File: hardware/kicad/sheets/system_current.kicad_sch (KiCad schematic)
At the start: 5 parts, among them U23 INA237AIDGSR

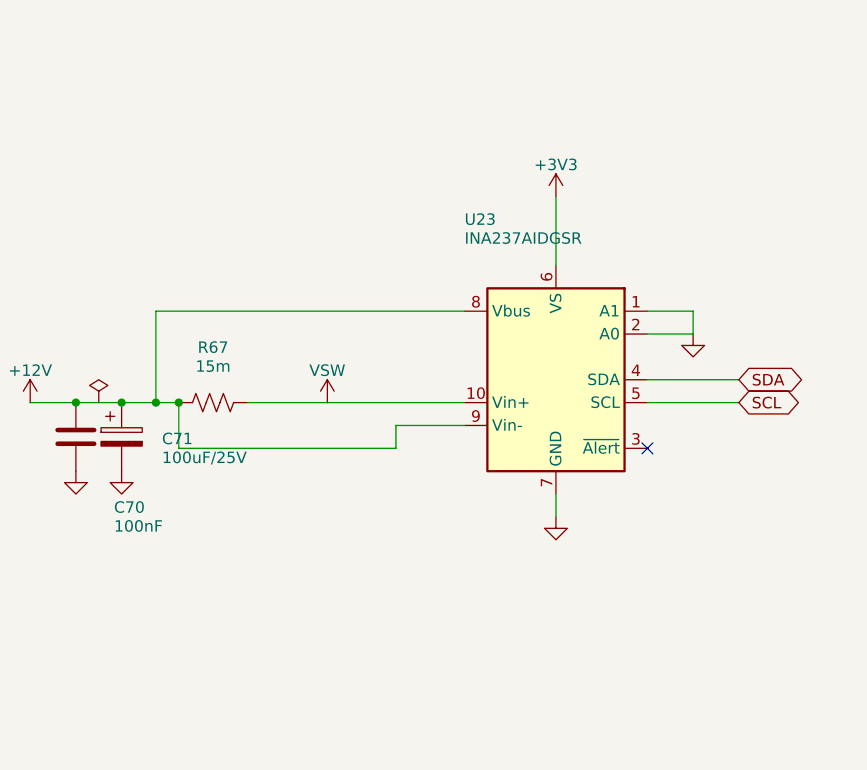
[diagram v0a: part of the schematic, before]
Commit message: Put supply pins on top and grounds on the bottom of IC symbols; flake8-clean Python
Schematic: re-laid out pins on U2, U3, U6, U7, U11, U14, U17-U20, U22-U24
and PS1 (supply on top, ground/strap pins on the bottom edge) via custom
`cryocooler:` symbols (make_lib.from_stock) and a gnd_bus helper; U18/U2
use mirroring instead of a 180 degree rotation. Nets are unchanged (ERC 0,
117/117 datasheet rules, PCB nets still match). Text placement now shows
every power-symbol name, avoids wires, and uses a realistic character width.

Python: black -l 79 -S plus manual wrapping so hardware/kicad and scripts/
pass flake8; add .flake8.

Co-Authored-By: Claude Sonnet 5.5 <noreply@anthropic.com>
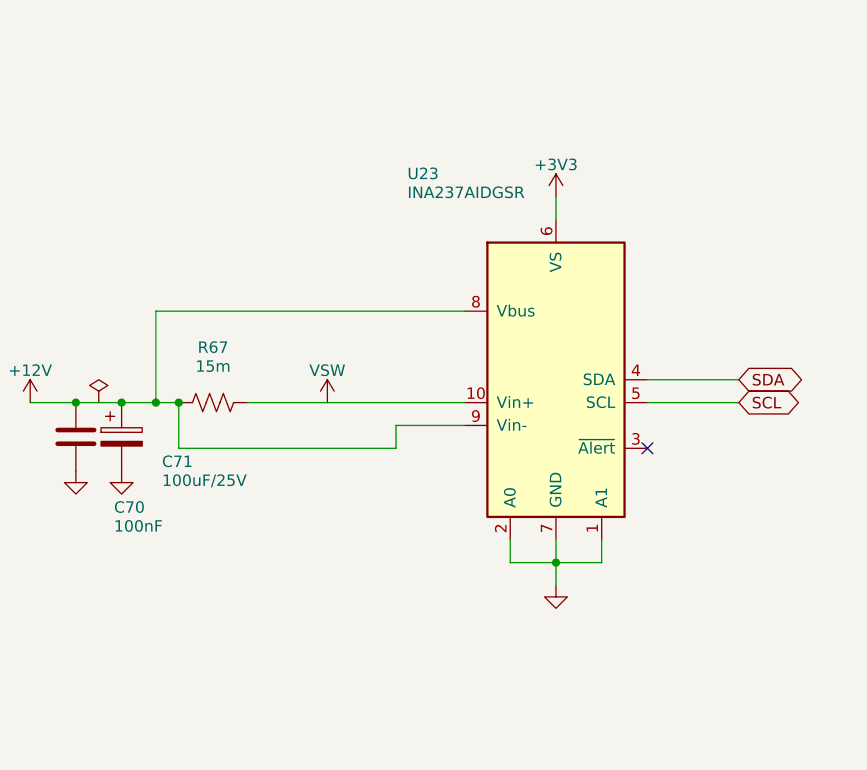
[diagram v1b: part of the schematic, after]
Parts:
- removed C70: 100nF, Capacitor_SMD:C_0805_2012Metric, symbol Device:C
- removed C72: 100nF, Capacitor_SMD:C_0603_1608Metric, symbol Device:C
- added C71: 100uF/25V, Capacitor_SMD:CP_Elec_8x10, symbol Device:C_Polarized
- added U23: INA237AIDGSR, Package_SO:TSSOP-10_3x3mm_P0.5mm, symbol cryocooler:INA237
- C70: renamed from U23; value INA237AIDGSR -> 100nF; footprint Package_SO:TSSOP-10_3x3mm_P0.5mm -> Capacitor_SMD:C_0805_2012Metric; symbol Sensor_Energy:INA237 -> Device:C
- C72: renamed from C71; value 100uF/25V -> 100nF; footprint Capacitor_SMD:CP_Elec_8x10 -> Capacitor_SMD:C_0603_1608Metric; symbol Device:C_Polarized -> Device:C
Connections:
- net +12V: now also C70.1, C71.1, U23.8 (Vbus), U23.9 (Vin-); no longer C70.8 (Vbus), C70.9 (Vin-), C72.1
- net +3V3: now also C72.1, U23.6 (VS); no longer C70.6 (VS)
- net GND: now also C71.2, U23.1 (A1), U23.2 (A0), U23.7 (GND); no longer C70.1 (A1), C70.7 (GND)
- net SCL: now also U23.5 (SCL); no longer C70.5 (SCL)
- net SDA: now also U23.4 (SDA); no longer C70.4 (SDA)
- net VSW: now also U23.10 (Vin+); no longer C70.10 (Vin+)

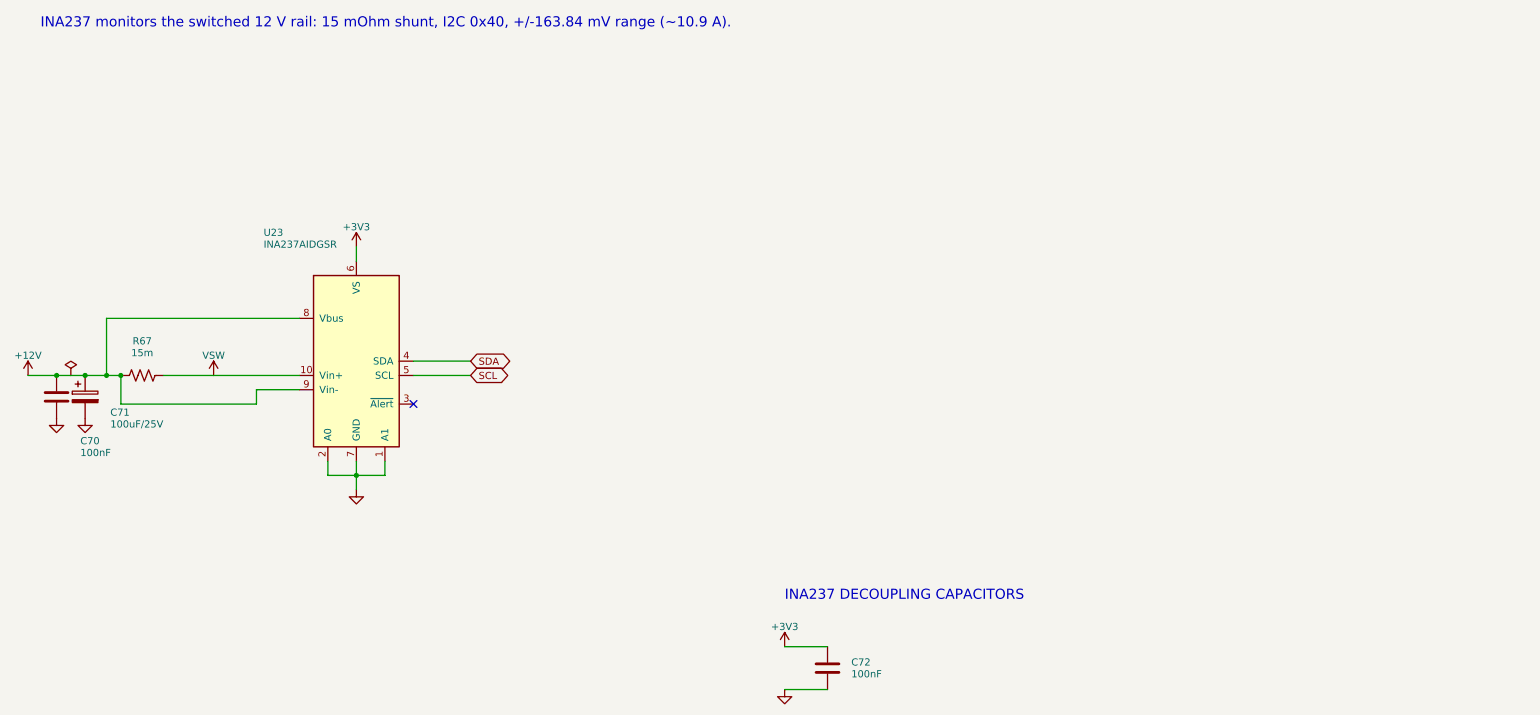
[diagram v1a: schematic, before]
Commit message: KiCad schematic: INA239, ADS1220, SC18IS604 bridge, relay driver, test points
- system_current: INA237 -> INA239 (SPI, CS GPIO3) with the 49.9 ohm / 470 nF
  input filter, power LED and ALERT LED; VBUS shares the filtered IN- node.
- cold_head: ADS122C04 -> ADS1220 (SPI, CS GPIO44).
- i2c_bridge (new): SC18IS604 SPI-to-I2C bridge for the EMC2303, with a
  74LVC1G125 gating its MISO onto the shared bus.
- compressor_relay (new): GPIO16 high-side switch sharing one generator
  function with the amplifier REM switch.
- debug (new): about 40 test points and rail LEDs (the isolated rail LED
  returns to ISO_GND).
- ISO7741 -> ACS37800 SPI lines are straight wires (pins reordered on the
  symbol); USB_VBUS is one wire plus a naming label.
- Custom symbols for INA239, ADS1220, SC18IS604; datasheet rules 117 -> 162;
  GPIO map checks updated. ERC 0.

Co-Authored-By: Claude Sonnet 5.5 <noreply@anthropic.com>
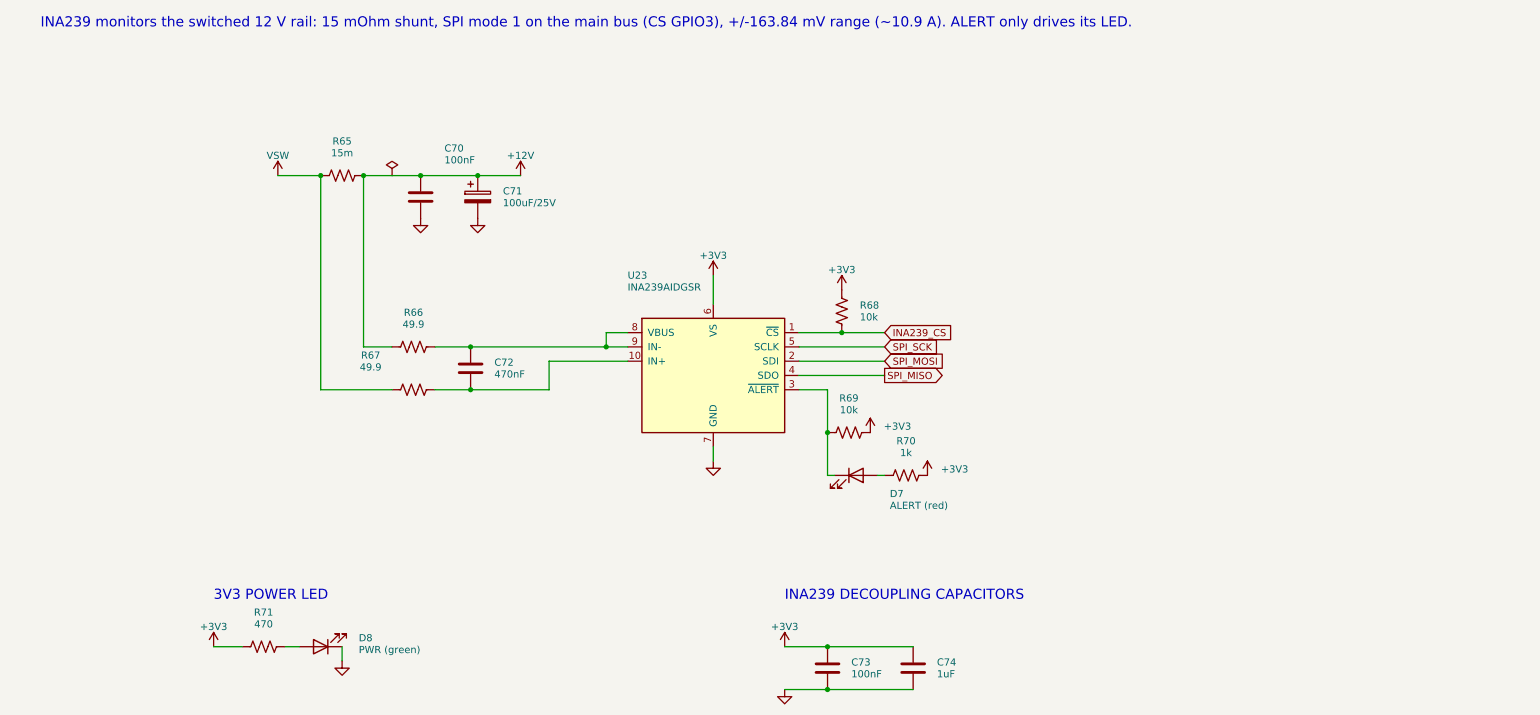
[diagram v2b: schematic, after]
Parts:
- removed R67: 15m, Resistor_SMD:R_2512_6332Metric, symbol Device:R_US
- removed U23: INA237AIDGSR, Package_SO:TSSOP-10_3x3mm_P0.5mm, symbol cryocooler:INA237
- added C71: 100uF/25V, Capacitor_SMD:CP_Elec_8x10, symbol Device:C_Polarized
- added C73: 100nF, Capacitor_SMD:C_0603_1608Metric, symbol Device:C
- added C74: 1uF, Capacitor_SMD:C_0805_2012Metric, symbol Device:C
- added D7: ALERT (red), LED_SMD:LED_0603_1608Metric, symbol Device:LED
- added D8: PWR (green), LED_SMD:LED_0603_1608Metric, symbol Device:LED
- added R65: 15m, Resistor_SMD:R_2512_6332Metric, symbol Device:R_US
- added R66: 49.9, Resistor_SMD:R_0603_1608Metric, symbol Device:R_US
- added R68, R69: 10k, Resistor_SMD:R_0603_1608Metric, symbol Device:R_US
- added R70: 1k, Resistor_SMD:R_0603_1608Metric, symbol Device:R_US
- added R71: 470, Resistor_SMD:R_0603_1608Metric, symbol Device:R_US
- added U23: INA239AIDGSR, Package_SO:TSSOP-10_3x3mm_P0.5mm, symbol cryocooler:INA239AIDGSR
- C72: value 100nF -> 470nF; footprint Capacitor_SMD:C_0603_1608Metric -> Capacitor_SMD:C_0805_2012Metric
- R67: renamed from C71; value 100uF/25V -> 49.9; footprint Capacitor_SMD:CP_Elec_8x10 -> Resistor_SMD:R_0603_1608Metric; symbol Device:C_Polarized -> Device:R_US
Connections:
- net +12V: now also C71.1, R65.2, R66.1; no longer R67.1
- net +3V3: now also C73.1, C74.1, R68.1, R69.2, R70.2, R71.1, U23.6 (VS); no longer C72.1
- net GND: now also C71.2, C73.2, C74.2, D8.1 (K), U23.7 (GND); no longer C72.2, R67.2
- net VSW: now also R67.1, R65.1
- new net: C72.2, R67.2, U23.10 (IN+)
- new net: D8.2 (A), R71.2
- new net: D7.2 (A), R70.1
- new net: C72.1, R66.2, U23.8 (VBUS), U23.9 (IN-)
- new net: D7.1 (K), R69.1, U23.3 (~{ALERT})
- new net INA239_CS: R68.2, U23.1 (~{CS})
- new net SPI_MISO: U23.4 (SDO)
- new net SPI_MOSI: U23.2 (SDI)
- new net SPI_SCK: U23.5 (SCLK)
- no-connect marks 1 -> 0
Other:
- note added: "3V3 POWER LED"
- note added: "INA239 DECOUPLING CAPACITORS"
- note added: "INA239 monitors the switched 12 V rail: 15 mOhm shunt, SPI mode 1 on the main bus (CS GPIO3), +/-163.84 mV range (~10.9 A). ALERT only drives its LED."
- note removed: "INA237 DECOUPLING CAPACITORS"
- note removed: "INA237 monitors the switched 12 V rail: 15 mOhm shunt, I2C 0x40, +/-163.84 mV range (~10.9 A)."
- moved on the sheet: R67

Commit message: Move the IMU off-board (J14) and add labelled module boxes to the PCB
The LSM6DSOX is now the Adafruit breakout (product 4438) mounted on the
cryocooler and cabled to a 10-pin JST XH header (J14) over the shared SPI
bus. U19 and its capacitors are gone; J14 and six 100 R series resistors
are added, and every other reference number is unchanged.

PCB (130 x 110 mm, was 130 x 100):
- one outlined, labelled silkscreen box per module (pcbfloorplan.py); the
  placer keeps parts inside their box and reserves a label pocket beside
  every part so each label sits next to its own part
- box 3D models for U3, L2, L3, F1 and PS1, whose library models are missing
- re-routed; DRC 0 errors, 0 unconnected; back logo recentred
- gen_pcb.py texts redoes the silkscreen on a routed board

Firmware: SPI clock constant for the module, comments updated; ambient
temperature now reads the cooler-body IMU temperature.

Docs, BOM and fabrication files regenerated.

Co-Authored-By: Claude Sonnet 5.5 <noreply@anthropic.com>
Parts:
- removed C71: 100uF/25V, Capacitor_SMD:CP_Elec_8x10, symbol Device:C_Polarized
- removed C72: 470nF, Capacitor_SMD:C_0805_2012Metric, symbol Device:C
- removed C73: 100nF, Capacitor_SMD:C_0603_1608Metric, symbol Device:C
- removed C74: 1uF, Capacitor_SMD:C_0805_2012Metric, symbol Device:C
- removed R66: 49.9, Resistor_SMD:R_0603_1608Metric, symbol Device:R_US
- added D8: PWR (green), LED_SMD:LED_0603_1608Metric, symbol Device:LED
- added R67: 49.9, Resistor_SMD:R_0603_1608Metric, symbol Device:R_US
- added R68: 10k, Resistor_SMD:R_0603_1608Metric, symbol Device:R_US
- added R70: 1k, Resistor_SMD:R_0603_1608Metric, symbol Device:R_US
- added R71: 470, Resistor_SMD:R_0603_1608Metric, symbol Device:R_US
- C71: renamed from R67; value 49.9 -> 100uF/25V; footprint Resistor_SMD:R_0603_1608Metric -> Capacitor_SMD:CP_Elec_8x10; symbol Device:R_US -> Device:C_Polarized
- C72: renamed from R69; value 10k -> 470nF; footprint Resistor_SMD:R_0603_1608Metric -> Capacitor_SMD:C_0805_2012Metric; symbol Device:R_US -> Device:C
- C73: renamed from R71; value 470 -> 100nF; footprint Resistor_SMD:R_0603_1608Metric -> Capacitor_SMD:C_0603_1608Metric; symbol Device:R_US -> Device:C
- C74: renamed from D8; value PWR (green) -> 1uF; footprint LED_SMD:LED_0603_1608Metric -> Capacitor_SMD:C_0805_2012Metric; symbol Device:LED -> Device:C
- R66: renamed from R68; value 10k -> 49.9
- R69: renamed from R70; value 1k -> 10k
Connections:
- net +12V: now also C71.1, R66.1
- net +3V3: now also C74.1, R68.1, R70.2, R71.1; no longer C72.2, R66.1
- net GND: now also C71.2, C73.2, C74.2, D8.1 (K); no longer C74.1 (K)
- net INA239_CS: now also R68.2; no longer R66.2
- net VSW: now also R67.1; no longer C71.1
- net at U23.10 (IN+): now also C72.2, R67.2; no longer C71.2
- net at R69.1: now also D7.1 (K), U23.3 (~{ALERT}); no longer D7.2 (A)
- net at U23.8 (VBUS), U23.9 (IN-): now also C72.1, R66.2
- new net: D8.2 (A), R71.2
- new net: D7.2 (A), R70.1
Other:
- moved on the sheet: C71, R66, R69

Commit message: Add per-section supply jumpers, 8-pin IMU header and connector pin labels
- Four 1.27 mm 2-pin jumpers (JP1-JP4), each with a rail-on LED, cut the
  supply of one section for debugging: signal generator +3V3, +-15V
  generator +5V in, isolated amp-current supply +5V in, and a shared
  +3V3 net for the cooling chips (EMC2303, RTD ADC, I2C bridge).
- J14 is now an 8-pin JST XH in the Adafruit LSM6DSOX pad order
  (VIN, GND, SCL, SDA, DO, CS, I1, I2); firmware pin comments updated.
- Pin-function labels beside every connector, "RAILS ±15V" box title.
- Board re-placed and re-routed (130 x 110 mm); DRC 0 errors, 0 unconnected,
  ERC 0, 173 datasheet rules pass. BOM, READMEs, Gerbers and renders
  regenerated; link_usb_vbus.py now adapts to the routed layout.

Co-Authored-By: Claude Sonnet 5.5 <noreply@anthropic.com>
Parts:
- removed C72: 470nF, Capacitor_SMD:C_0805_2012Metric, symbol Device:C
- removed D7: ALERT (red), LED_SMD:LED_0603_1608Metric, symbol Device:LED
- removed R71: 470, Resistor_SMD:R_0603_1608Metric, symbol Device:R_US
- added C70: 100nF, Capacitor_SMD:C_0805_2012Metric, symbol Device:C
- added C74: 1uF, Capacitor_SMD:C_0805_2012Metric, symbol Device:C
- added R67: 49.9, Resistor_SMD:R_0603_1608Metric, symbol Device:R_US
- C71: renamed from C70; value 100nF -> 100uF/25V; footprint Capacitor_SMD:C_0805_2012Metric -> Capacitor_SMD:CP_Elec_8x10; symbol Device:C -> Device:C_Polarized
- C72: renamed from R66; value 49.9 -> 470nF; footprint Resistor_SMD:R_0603_1608Metric -> Capacitor_SMD:C_0805_2012Metric; symbol Device:R_US -> Device:C
- D7: renamed from R69; value 10k -> ALERT (red); footprint Resistor_SMD:R_0603_1608Metric -> LED_SMD:LED_0603_1608Metric; symbol Device:R_US -> Device:LED
- R66: renamed from C71; value 100uF/25V -> 49.9; footprint Capacitor_SMD:CP_Elec_8x10 -> Resistor_SMD:R_0603_1608Metric; symbol Device:C_Polarized -> Device:R_US
- R68: renamed from R67; value 49.9 -> 10k
- R71: renamed from C74; value 1uF -> 470; footprint Capacitor_SMD:C_0805_2012Metric -> Resistor_SMD:R_0603_1608Metric; symbol Device:C -> Device:R_US
- renumbered R68 to R69
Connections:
- net +12V: now also C70.1; no longer C72.1
- net +3V3: now also R68.1, R69.2, C74.1; no longer D7.2, R69.1
- net GND: now also C70.2, C74.2; no longer R66.2, R71.2
- net INA239_CS: now also R68.2; no longer R69.2
- net VSW: now also R67.1; no longer R68.1
- net at D7.1 (K), U23.3 (~{ALERT}): now also R69.1
- net at D8.2 (A): now also R71.2
- net at R70.1: now also D7.2 (A)
- net at U23.10 (IN+): now also C72.2, R67.2; no longer R68.2
- net at U23.8 (VBUS), U23.9 (IN-): now also C72.1, R66.2; no longer C72.2
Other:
- moved on the sheet: D7, R66, R68, R69
